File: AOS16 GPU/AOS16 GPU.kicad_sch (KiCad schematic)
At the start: 10 parts

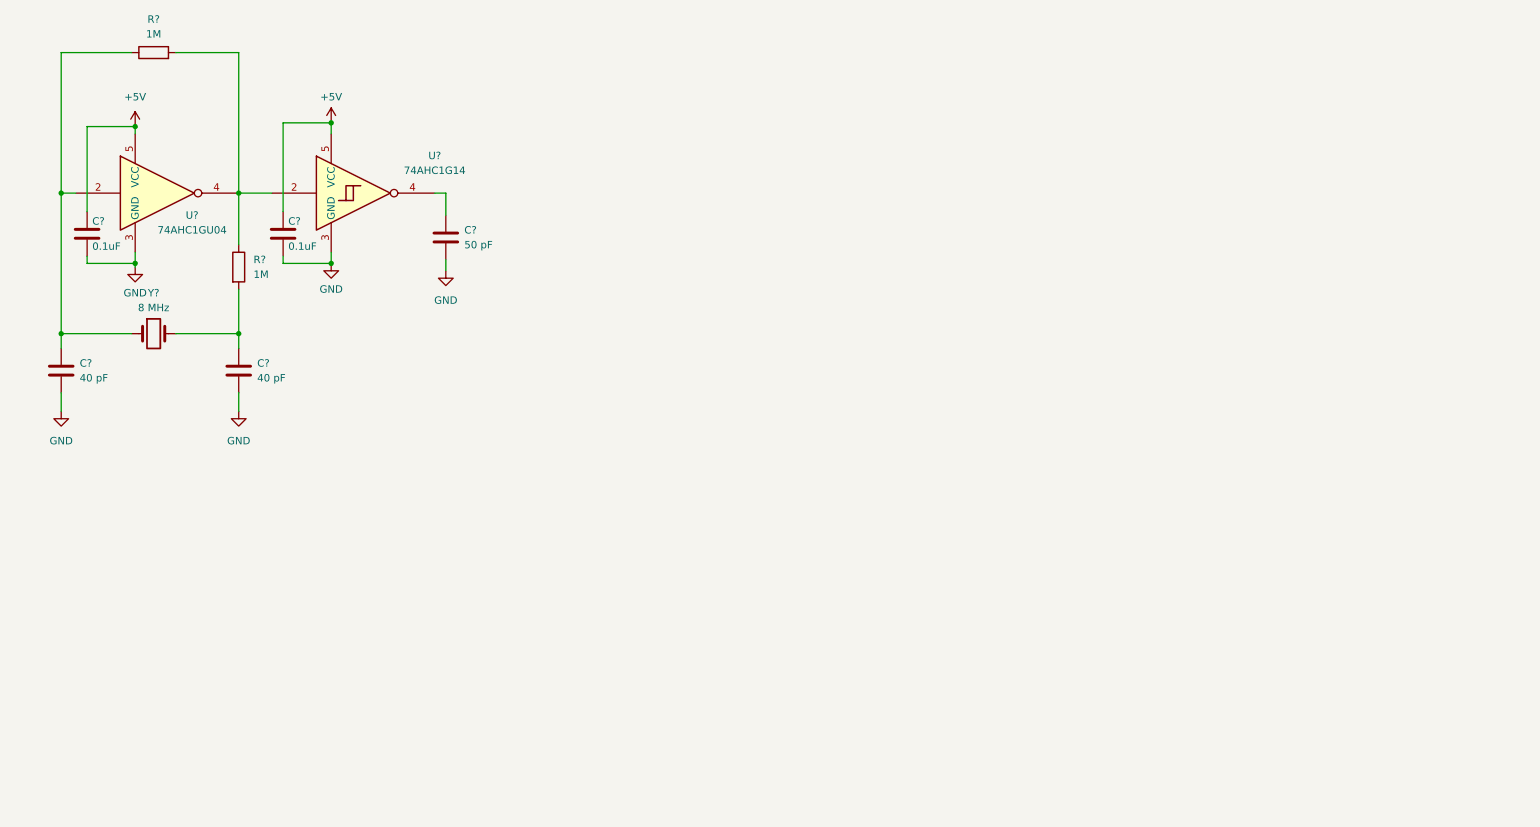
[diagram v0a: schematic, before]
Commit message: Added horizontal counting circuit
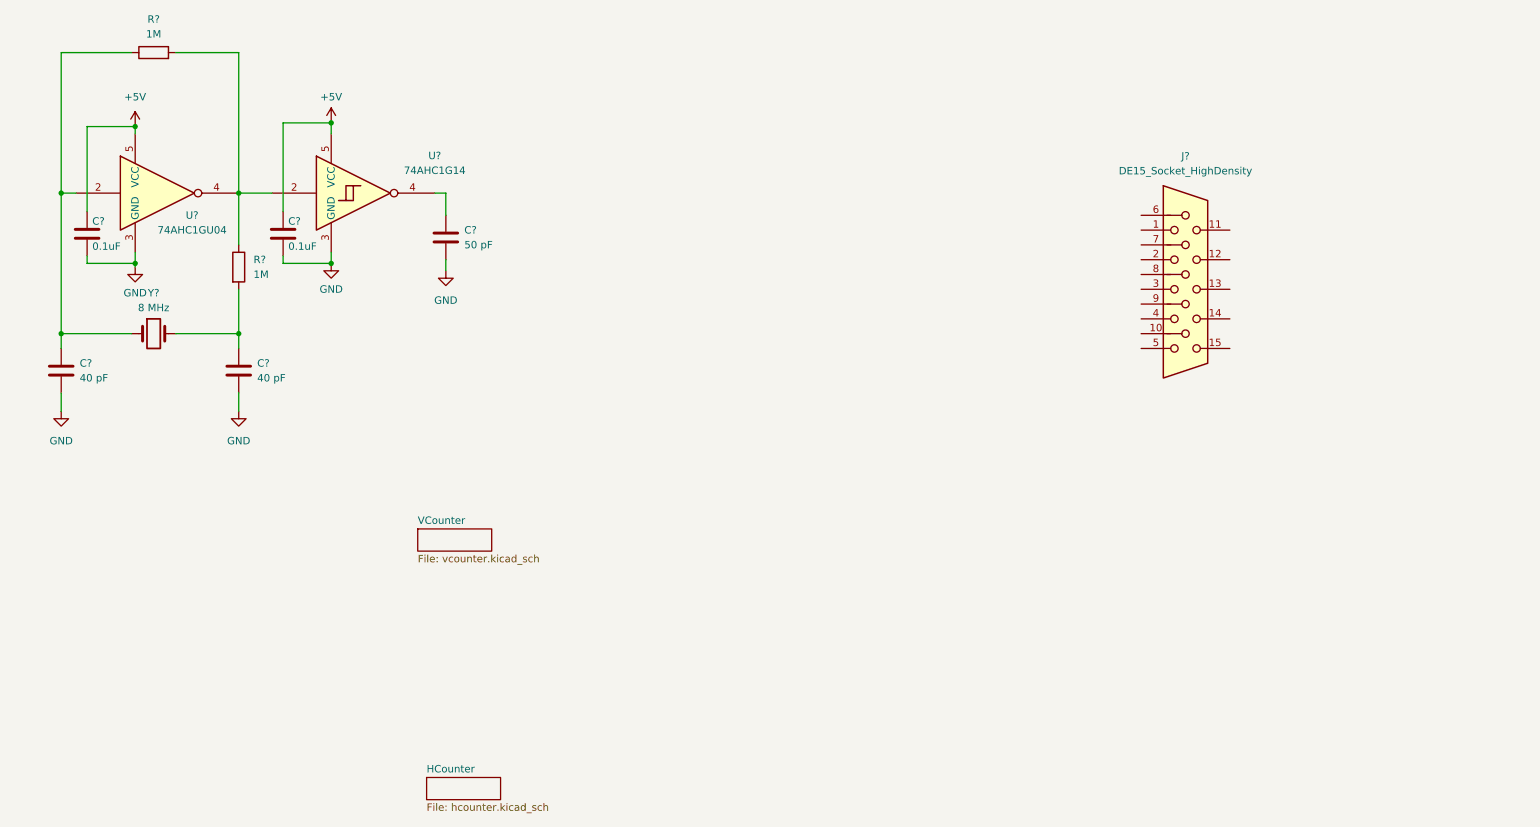
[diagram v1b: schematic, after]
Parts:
- added J?: DE15_Socket_HighDensity, symbol Connector:DE15_Socket_HighDensity
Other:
- added sheet HCounter (hcounter.kicad_sch)
- added sheet VCounter (vcounter.kicad_sch)
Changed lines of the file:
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@@
+	)
+	(symbol
+		(lib_id "Connector:DE15_Socket_HighDensity")
+		(at 213.36 62.23 0)
+		(unit 1)
+		(exclude_from_sim no)
+		(in_bom yes)
+		(on_board yes)
+		(dnp no)
+		(fields_autoplaced yes)
+		(property "Reference" "J?"
+			(at 213.36 39.37 0)
+			(effects
+				(font
+					(size 1.27 1.27)
+				)
+			)
+		)
+		(property "Value" "DE15_Socket_HighDensity"
+			(at 213.36 41.91 0)
+			(effects
+				(font
+					(size 1.27 1.27)
+				)
+			)
+		)
+		(property "Footprint" ""
+			(at 189.23 52.07 0)
+			(effects
+				(font
+					(size 1.27 1.27)
+				)
+				(hide yes)
+			)
+		)
+		(property "Datasheet" "~"
+			(at 189.23 52.07 0)
+			(effects
+				(font
+					(size 1.27 1.27)
+				)
+				(hide yes)
+			)
+		)
+		(property "Description" "15-pin D-SUB connector, socket (female), High density (3 columns), Triple Row, Generic, VGA-connector"
+			(at 213.36 62.23 0)
+			(effects
+				(font
+					(size 1.27 1.27)
+				)
+				(hide yes)
+			)
+		)
+		(pin "6"
+		)
+		(pin "8"
+		)
+		(pin "3"
+		)
+		(pin "11"
+		)
+		(pin "13"
+		)
+		(pin "14"
+		)
+		(pin "2"
+		)
+		(pin "4"
+		)
+		(pin "12"
+		)
+		(pin "1"
+		)
+		(pin "9"
+		)
+		(pin "7"
+		)
+		(pin "10"
+		)
+		(pin "5"
+		)
+		(pin "15"
+		)
+		(instances
+			(project ""
+				(path "/30867551-fb5e-4d50-9b6f-10252ea432a0"
+					(reference "J?")
+					(unit 1)
+				)
+			)
+		)
 	)
 	(symbol
@@
 				)
 			)
+		)
+	)
+	(sheet
+		(at 83.058 146.05)
+		(size 12.7 3.81)
+		(exclude_from_sim no)
+		(in_bom yes)
+		(on_board yes)
+		(dnp no)
+		(fields_autoplaced yes)
+		(stroke
+			(width 0.1524)
+			(type solid)
+		)
+		(fill
+			(color 0 0 0 0.0000)
+		)
+		(property "Sheetname" "HCounter"
+			(at 83.058 145.3384 0)
+			(effects
+				(font
+					(size 1.27 1.27)
+				)
+				(justify left bottom)
+			)
+		)
+		(property "Sheetfile" "hcounter.kicad_sch"
+			(at 83.058 150.4446 0)
+			(effects
+				(font
+					(size 1.27 1.27)
+				)
+				(justify left top)
+			)
+		)
+		(instances
+			(project "AOS16 GPU"
+				(path "/30867551-fb5e-4d50-9b6f-10252ea432a0"
+					(page "2")
+				)
+			)
+		)
+	)
+	(sheet
+		(at 81.534 103.378)
+		(size 12.7 3.81)
+		(exclude_from_sim no)
+		(in_bom yes)
+		(on_board yes)
+		(dnp no)
+		(fields_autoplaced yes)
+		(stroke
+			(width 0.1524)
+			(type solid)
+		)
+		(fill
+			(color 0 0 0 0.0000)
+		)
+		(property "Sheetname" "VCounter"
+			(at 81.534 102.6664 0)
+			(effects
+				(font
+					(size 1.27 1.27)
+				)
+				(justify left bottom)
+			)
+		)
+		(property "Sheetfile" "vcounter.kicad_sch"
+			(at 81.534 107.7726 0)
+			(effects
+				(font
+					(size 1.27 1.27)
+				)
+				(justify left top)
+			)
+		)
+		(instances
+			(project "AOS16 GPU"
+				(path "/30867551-fb5e-4d50-9b6f-10252ea432a0"
+					(page "3")
+				)
+			)

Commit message: Completed GPU schematic
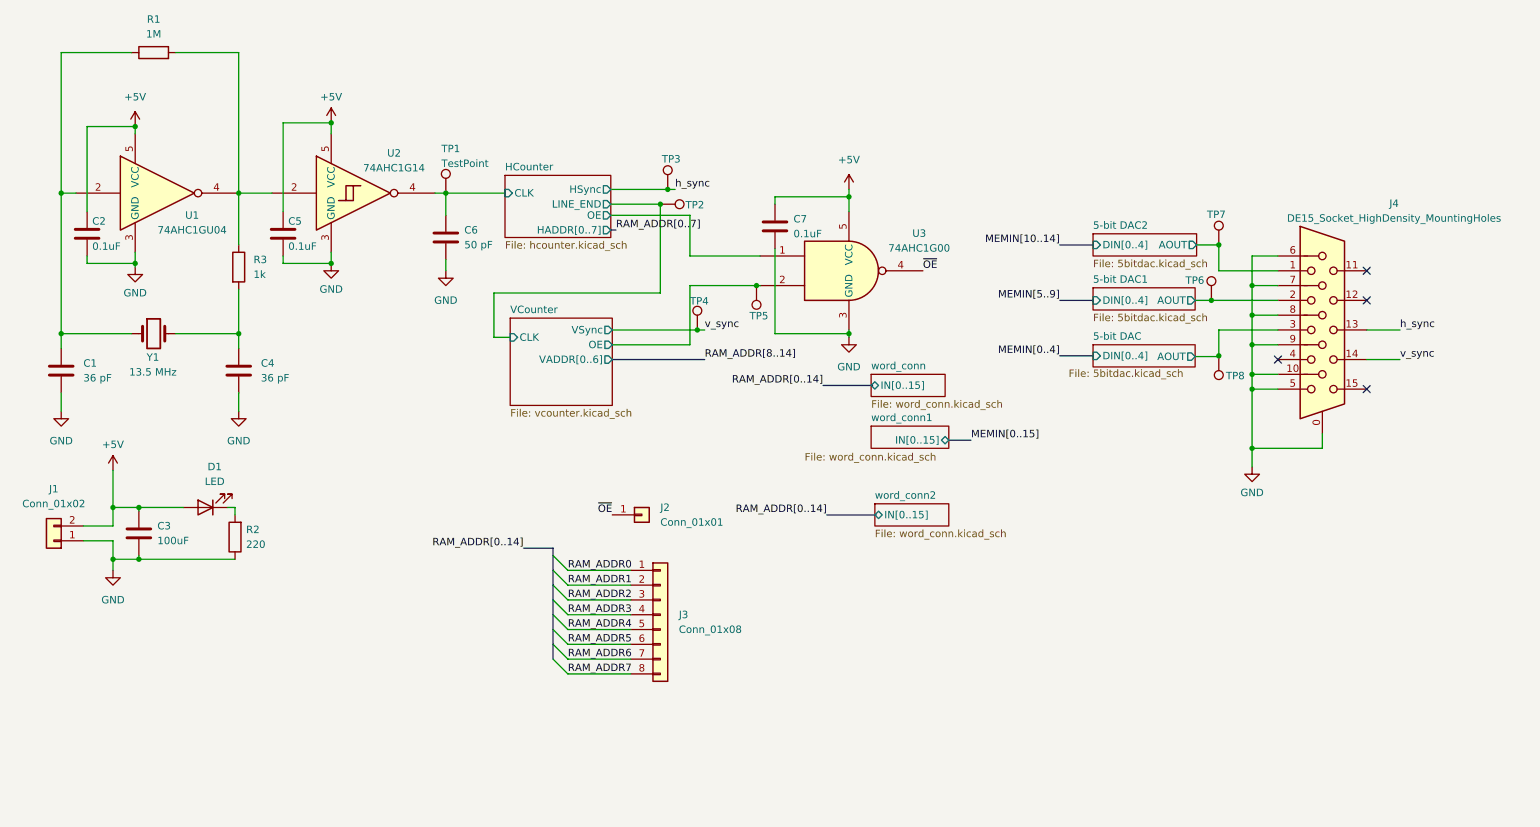
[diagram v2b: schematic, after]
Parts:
- removed J?: DE15_Socket_HighDensity, symbol Connector:DE15_Socket_HighDensity
- added C3: 100uF, Capacitor_SMD:CP_Elec_5x5.3, symbol Device:C
- added C7: 0.1uF, Capacitor_SMD:C_0603_1608Metric, symbol Device:C
- added D1: LED, LED_SMD:LED_0603_1608Metric, symbol Device:LED
- added J1: Conn_01x02, Connector_PinHeader_2.54mm:PinHeader_1x02_P2.54mm_Vertical, symbol Connector_Generic:Conn_01x02
- added J2: Conn_01x01, Connector_PinHeader_2.54mm:PinHeader_1x01_P2.54mm_Vertical, symbol Connector_Generic:Conn_01x01
- added J3: Conn_01x08, Connector_PinHeader_2.54mm:PinHeader_1x08_P2.54mm_Vertical, symbol Connector_Generic:Conn_01x08
- added J4: DE15_Socket_HighDensity_MountingHoles, Connector_Dsub:DSUB-15-HD_Socket_Horizontal_P2.29x1.90mm_EdgePinOffset3.03mm_Housed_MountingHolesOffset4.94mm, symbol Connector:DE15_Socket_HighDensity_MountingHoles
- added R2: 220, Resistor_SMD:R_0201_0603Metric, symbol Device:R
- added TP1, TP2, TP3, TP4, TP5, TP6, TP7, TP8: TestPoint, TestPoint:TestPoint_Pad_D2.0mm, symbol Connector:TestPoint
- added U3: 74AHC1G00, Package_TO_SOT_SMD:SOT-23-5, symbol 74xGxx:74AHC1G00
- C1, C4: renamed from C?; value 40 pF -> 36 pF; footprint (none) -> Capacitor_SMD:C_0603_1608Metric
- C2, C5, C6: renamed from C?; footprint (none) -> Capacitor_SMD:C_0603_1608Metric
- R1: renamed from R?; footprint (none) -> Resistor_SMD:R_0603_1608Metric
- R3: renamed from R?; value 1M -> 1k; footprint (none) -> Resistor_SMD:R_0603_1608Metric
- U1, U2: renamed from U?; footprint (none) -> Package_TO_SOT_SMD:SOT-23-5
- Y1: renamed from Y?; value 8 MHz -> 13.5 MHz; footprint (none) -> Crystal:Crystal_SMD_HC49-SD
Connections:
- net +5V: now also C3.1, C7.1, D1.2 (A), J1.2 (Pin_2), U3.5 (VCC)
- net GND: now also C3.2, C7.2, J1.1 (Pin_1), J4.0, J4.10, J4.5, J4.6, J4.7, J4.8, J4.9, R2.1, U3.3 (GND)
- net HCounter/CLK: now reaches C6.1, U2.4
- net HCounter/CLK: now also TP1.1
- new net: D1.1 (K), R2.2
- new net 5-bit DAC/AOUT: J4.3, TP8.1
- new net 5-bit DAC1/AOUT: J4.2, TP6.1
- new net 5-bit DAC2/AOUT: J4.1, TP7.1
- new net HCounter/LINE_END: TP2.1
- new net HCounter/OE: U3.1
- new net RAM_ADDR0: J3.1 (Pin_1)
- new net RAM_ADDR1: J3.2 (Pin_2)
- new net RAM_ADDR2: J3.3 (Pin_3)
- new net RAM_ADDR3: J3.4 (Pin_4)
- new net RAM_ADDR4: J3.5 (Pin_5)
- new net RAM_ADDR5: J3.6 (Pin_6)
- new net RAM_ADDR6: J3.7 (Pin_7)
- new net RAM_ADDR7: J3.8 (Pin_8)
- new net VCounter/OE: TP5.1, U3.2
- new net h_sync: J4.13, TP3.1
- new net v_sync: J4.14, TP4.1
- new net ~{OE}: J2.1 (Pin_1), U3.4
- no-connect marks 0 -> 4
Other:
- added sheet 5-bit DAC (5bitdac.kicad_sch)
- added sheet 5-bit DAC1 (5bitdac.kicad_sch)
- added sheet 5-bit DAC2 (5bitdac.kicad_sch)
- added sheet word_conn (word_conn.kicad_sch)
- added sheet word_conn1 (word_conn.kicad_sch)
- added sheet word_conn2 (word_conn.kicad_sch)
- sheet HCounter ports: added CLK, HADDR[0..7], HSync, LINE_END, OE; removed none
- sheet VCounter ports: added CLK, OE, VADDR[0..6], VSync; removed none

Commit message: GPU PCB Design v1
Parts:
- removed C5: 0.1uF, Capacitor_SMD:C_0603_1608Metric, symbol Device:C
- removed J3: Conn_01x08, Connector_PinHeader_2.54mm:PinHeader_1x08_P2.54mm_Vertical, symbol Connector_Generic:Conn_01x08
- removed U1: 74AHC1GU04, Package_TO_SOT_SMD:SOT-23-5, symbol 74xGxx:74AHC1GU04
- removed U2: 74AHC1G14, Package_TO_SOT_SMD:SOT-23-5, symbol 74xGxx:74AHC1G14
- added U1: 74AHC1G14, Package_TO_SOT_SMD:SOT-23-5, symbol 74xGxx:74AHC1G14
- added U25: 74HC00, Package_SO:SOIC-14_3.9x8.7mm_P1.27mm, symbol 74xx:74HC00
- added U6: 74AHC04, Package_SO:SOIC-14_3.9x8.7mm_P1.27mm, symbol 74xx:74AHC04
- R2: footprint Resistor_SMD:R_0201_0603Metric -> Resistor_SMD:R_0603_1608Metric
- Y1: value 13.5 MHz -> 18 MHz; footprint Crystal:Crystal_SMD_HC49-SD -> Crystal:Crystal_HC49-4H_Vertical
- renumbered C6 to C5, C7 to C6, J4 to J3, U3 to U2
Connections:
- net +5V: now also U1.5 (VCC)
- net GND: now also U1.3 (GND)
- net 18mhz: now reaches R1.2, R3.1
- net 18mhz: now also U1.4, U25.2, U25.5
- net at C1.1, R1.1, Y1.1: now also U1.2
- net HCounter/CLK renamed 9mhz
- net 9mhz: now also U25.11, U25.9
- new net: U25.4, U6.8
- new net: U25.1, U25.13, U25.8, U6.9
- new net: U25.10, U25.6
- new net: U25.12, U25.3
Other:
- removed sheet word_conn2

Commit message: updated gpu
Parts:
- removed C1, C4: 36 pF, Capacitor_SMD:C_0603_1608Metric, symbol Device:C
- removed C2: 0.1uF, Capacitor_SMD:C_0603_1608Metric, symbol Device:C
- removed C5: 50 pF, Capacitor_SMD:C_0603_1608Metric, symbol Device:C
- removed R1: 1M, Resistor_SMD:R_0603_1608Metric, symbol Device:R
- removed R3: 1k, Resistor_SMD:R_0603_1608Metric, symbol Device:R
- removed U1: 74AHC1G14, Package_TO_SOT_SMD:SOT-23-5, symbol 74xGxx:74AHC1G14
- removed U25: 74HC00, Package_SO:SOIC-14_3.9x8.7mm_P1.27mm, symbol 74xx:74HC00
- removed U6: 74AHC04, Package_SO:SOIC-14_3.9x8.7mm_P1.27mm, symbol 74xx:74AHC04
- removed Y1: 18 MHz, Crystal:Crystal_HC49-4H_Vertical, symbol Device:Crystal
- added C28, C29, C30: 0.1uF, Capacitor_SMD:C_0603_1608Metric, symbol Device:C_Small
- added D4: LED_Small, LED_SMD:LED_0603_1608Metric, symbol Device:LED_Small
- added J6: Conn_01x01, Connector_PinHeader_2.54mm:PinHeader_1x01_P2.54mm_Vertical, symbol Connector_Generic:Conn_01x01
- added J7: Conn_Coaxial, Connector_Coaxial:SMA_Amphenol_132289_EdgeMount, symbol Connector:Conn_Coaxial
- added R40: 220, Resistor_SMD:R_0603_1608Metric, symbol Device:R_Small
- added TP10, TP9: TestPoint, TestPoint:TestPoint_Pad_D2.0mm, symbol Connector:TestPoint
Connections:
- net +5V: now also C28.1, C29.1, C30.1
- net 9mhz: now also J6.1 (Pin_1), J7.1 (In)
- net GND: now also C28.2, C29.2, C30.2, J7.2 (Ext), R40.2
- net HCounter/OE: now also TP9.1
- net ~{OE}: now also D4.2 (A), TP10.1
- new net: D4.1 (K), R40.1
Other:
- note added: "BLUE"
- note added: "GREEN"
- note added: "RED"
- moved on the sheet: TP7, TP8
